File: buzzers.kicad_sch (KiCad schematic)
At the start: 10 parts, among them SW1 OFF/ON

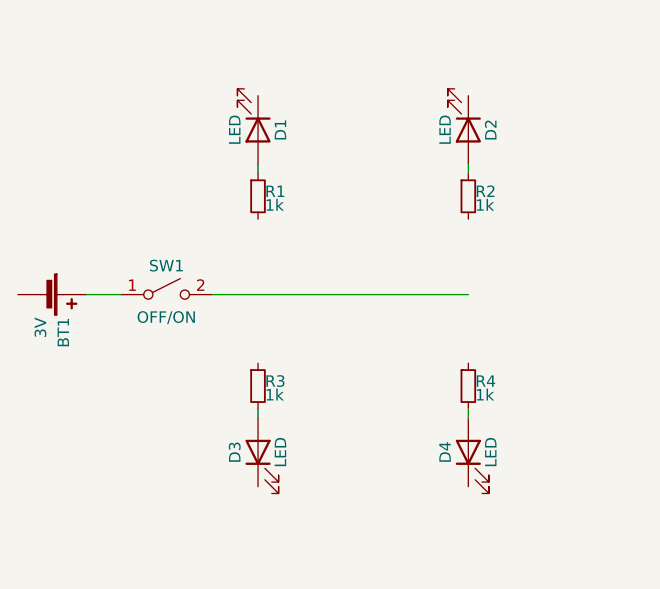
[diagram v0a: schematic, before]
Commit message: Added RCA connectors
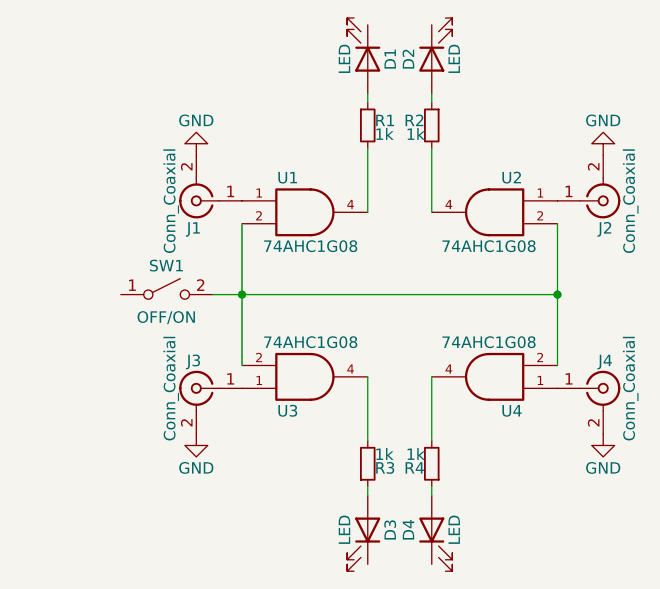
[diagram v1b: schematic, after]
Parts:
- removed BT1: 3V, symbol Device:Battery_Cell
- added J1, J2, J3, J4: Conn_Coaxial, symbol Connector:Conn_Coaxial
- added U1, U2, U3, U4: 74AHC1G08, symbol 74xGxx:74AHC1G08
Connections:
- net at R4.2: now also U4.4; no longer D4.2 (A)
- net at R1.2: now also U1.4
- net at R3.1: now also D3.2 (A)
- net at R3.2: now also U3.4; no longer D3.2 (A)
- net at SW1.2 (B): now also U1.2, U2.2, U3.2, U4.2
- net at R2.2: now also U2.4
- net at R4.1: now also D4.2 (A)
- new net: J2.1 (In), U2.1
- new net: J4.1 (In), U4.1
- new net: J3.1 (In), U3.1
- new net: J1.1 (In), U1.1
- new net GND: J1.2 (Ext), J2.2 (Ext), J3.2 (Ext), J4.2 (Ext), U1.3 (GND), U2.3 (GND), U3.3 (GND), U4.3 (GND)
- new net VCC: U1.5 (VCC), U2.5 (VCC), U3.5 (VCC), U4.5 (VCC)
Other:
- moved on the sheet: D1, R1
